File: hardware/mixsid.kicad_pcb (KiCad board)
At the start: 2 copper layers, 61 x 55.9 mm, 69 parts, among them P1 INPUT, P2 CONTROL, P4 SOCKET LEFT, P5 OUTPUT, P6 SOCKET RIGHT, Q1 BC547, Q2 BC547, U1 GAL16V8, U2 SID2, U3 7812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

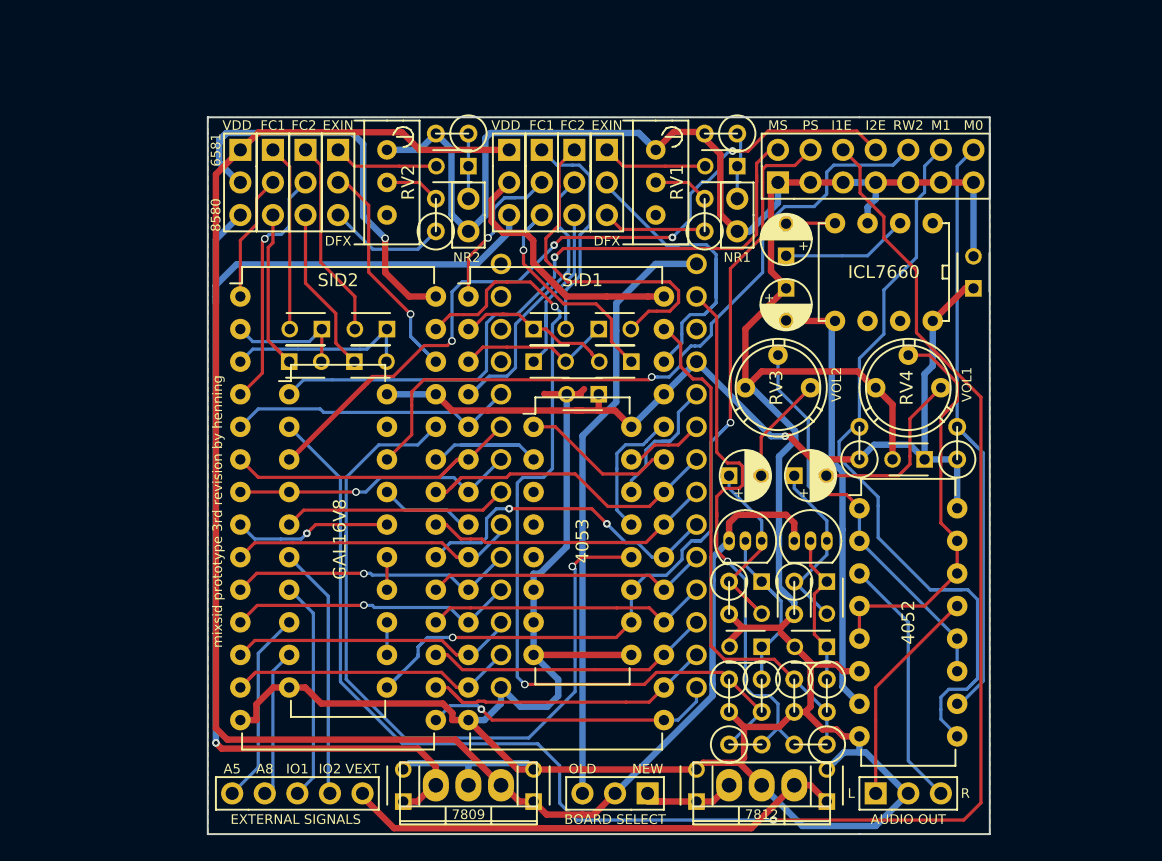
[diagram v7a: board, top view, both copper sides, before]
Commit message: Hardware: Improved silkscreen
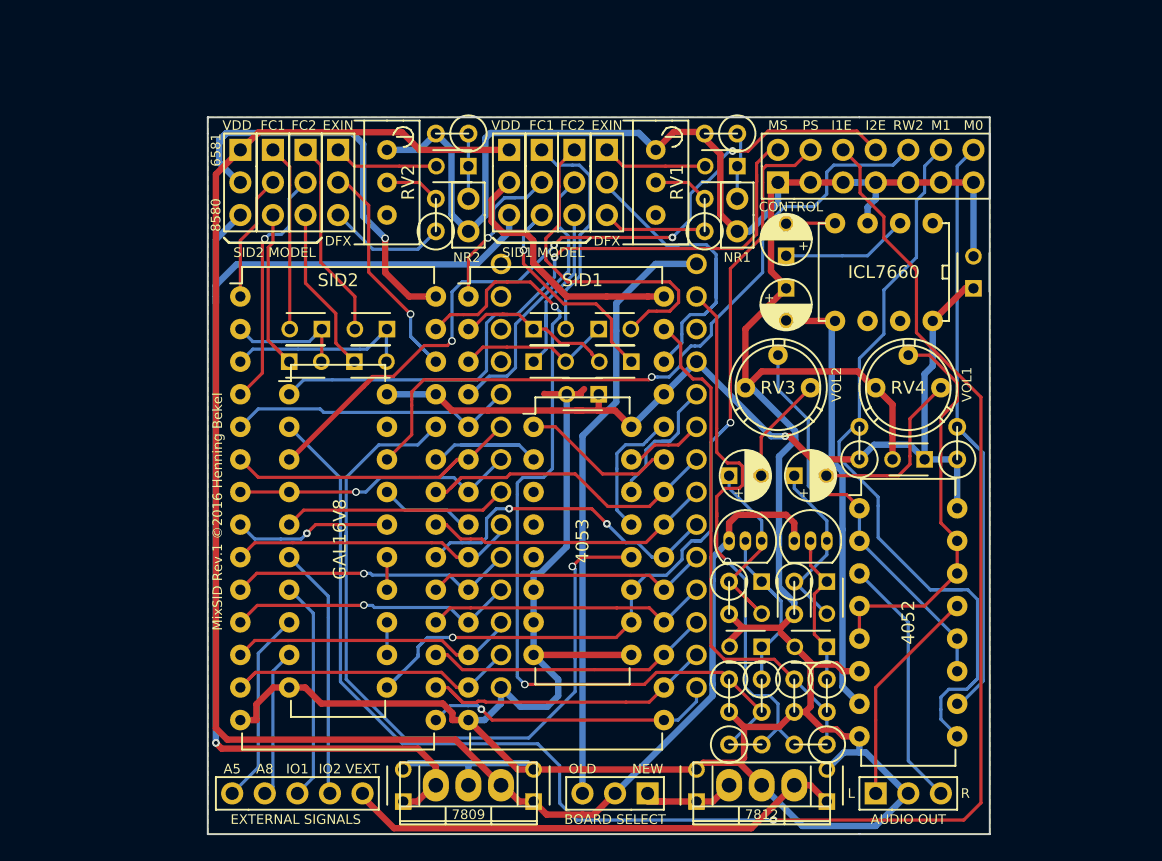
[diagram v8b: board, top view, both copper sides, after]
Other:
- board text added: "CONTROL"
- board text added: "MixSID Rev.1 ©2016 Henning Bekel"
- board text added: "SID1 MODEL"
- board text added: "SID2 MODEL"
- board text removed: "mixsid prototype 3rd revision by henning"
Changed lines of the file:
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@@
     (area 128.194999 67.234999 189.305001 123.265001)
     (thickness 1.6)
-    (drawings 47)
+    (drawings 56)
     (tracks 1077)
     (zones 0)
@@
   (page A4)
   (layers
-    (0 F.Cu signal)
-    (31 B.Cu signal)
+    (0 F.Cu signal hide)
+    (31 B.Cu signal hide)
     (32 B.Adhes user)
     (33 F.Adhes user)
@@
     (descr "5/16, Round, Trimming, Potentiometer, Bourns, 3339")
     (tags "5/16, Round, Trimming, Potentiometer, Bourns, 3339")
-    (fp_text reference RV3 (at 2.413 0 90) (layer F.SilkS)
+    (fp_text reference RV3 (at 2.54 0 180) (layer F.SilkS)
       (effects (font (size 1 1) (thickness 0.15)))
     )
@@
     (descr "5/16, Round, Trimming, Potentiometer, Bourns, 3339")
     (tags "5/16, Round, Trimming, Potentiometer, Bourns, 3339")
-    (fp_text reference RV4 (at 2.413 0 90) (layer F.SilkS)
+    (fp_text reference RV4 (at 2.54 0 180) (layer F.SilkS)
       (effects (font (size 1 1) (thickness 0.15)))
     )
@@
     )
   )
-  (gr_text "mixsid prototype 3rd revision by henning" (at 129.032 98.044 90) (layer F.SilkS)
+  (gr_text CONTROL (at 173.736 74.295) (layer F.SilkS)
     (effects (font (size 0.75 0.75) (thickness 0.15)))
   )
+  (gr_line (start 150.495 76.708) (end 150.876 77.089) (angle 90) (layer F.SilkS) (width 0.2))
+  (gr_line (start 158.115 76.708) (end 157.734 77.089) (angle 90) (layer F.SilkS) (width 0.2))
+  (gr_line (start 157.734 77.089) (end 150.876 77.089) (angle 90) (layer F.SilkS) (width 0.2))
+  (gr_text "SID1 MODEL" (at 154.432 77.851) (layer F.SilkS)
+    (effects (font (size 0.75 0.75) (thickness 0.15)))
+  )
+  (gr_text "SID2 MODEL" (at 133.477 77.851) (layer F.SilkS)
+    (effects (font (size 0.75 0.75) (thickness 0.15)))
+  )
+  (gr_line (start 136.779 77.089) (end 129.921 77.089) (angle 90) (layer F.SilkS) (width 0.2))
+  (gr_line (start 137.16 76.708) (end 136.779 77.089) (angle 90) (layer F.SilkS) (width 0.2))
+  (gr_line (start 129.54 76.708) (end 129.921 77.089) (angle 90) (layer F.SilkS) (width 0.2))
+  (gr_text "MixSID Rev.1 ©2016 Henning Bekel" (at 129.032 98.044 90) (layer F.SilkS)
+    (effects (font (size 0.75 0.75) (thickness 0.15)))
+  )
